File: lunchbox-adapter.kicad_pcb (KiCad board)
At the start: 2 copper layers, 67.6 x 89.2 mm, 91 parts, among them J1 Conn_01x24, J3 Conn_01x03, J4 Conn_01x03, J5 Conn_01x03, J6 Conn_01x06, J7 Conn_01x06, J8 Conn_01x03, Q1 SMBTA42, Q10 SMBTA42, Q11 SMBTA42, Q12 SMBTA42, Q2 SMBTA42, Q3 SMBTA42, Q4 SMBTA42, Q5 BCP51, Q6 SMBTA42, Q7 SMBTA42, Q8 SMBTA42, Q9 SMBTA42, U1 HCF4028B, U2 LM1117-5.0, U3 LM2904

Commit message: finished pcb design
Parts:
- turned C3 to 270 degrees
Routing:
- net START_BUTTON: track 57.9 -> 77.4 mm, vias 1 -> 2
- net GEAR_BCD_B: track 50.1 -> 65.8 mm, vias 1 -> 2
- net GEAR_BCD_A: track 49.3 -> 62.1 mm, vias 1 -> 2
- net +12V: track 75.0 -> 62.4 mm, vias 12 -> 16
- net SPD_12V: track 114.7 -> 124.8 mm, vias 1 -> 4
- net GEAR_BCD_C: track 50.4 -> 59.6 mm, vias 1 -> 2
- net Net-(J1-Pad15): track 25.9 -> 34.9 mm
- net SPEED_SENSOR: track 97.8 -> 105.5 mm, vias 1 -> 4
- net OIL_LAMP: track 75.8 -> 82.0 mm
- net SPD: track 10.6 -> 16.5 mm
- net VCC_Sensor: track 25.8 -> 20.5 mm, vias 1 -> 2
- net CHOKE_LAMP: track 76.3 -> 80.5 mm
- net RPM: track 16.5 -> 20.7 mm
- net TEMP_LAMP: track 76.4 -> 80.3 mm
- net GND: track 87.1 -> 90.3 mm
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
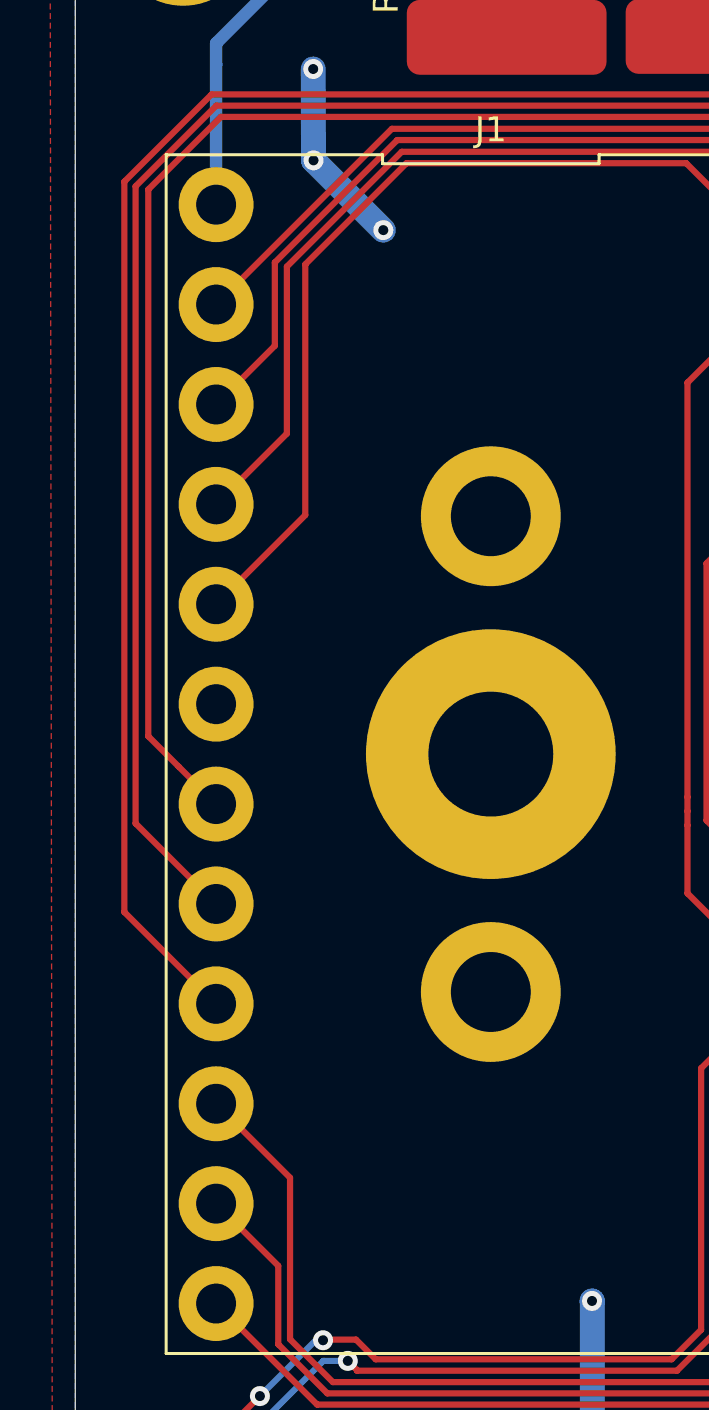
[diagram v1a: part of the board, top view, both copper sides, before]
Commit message: add schematic PDF
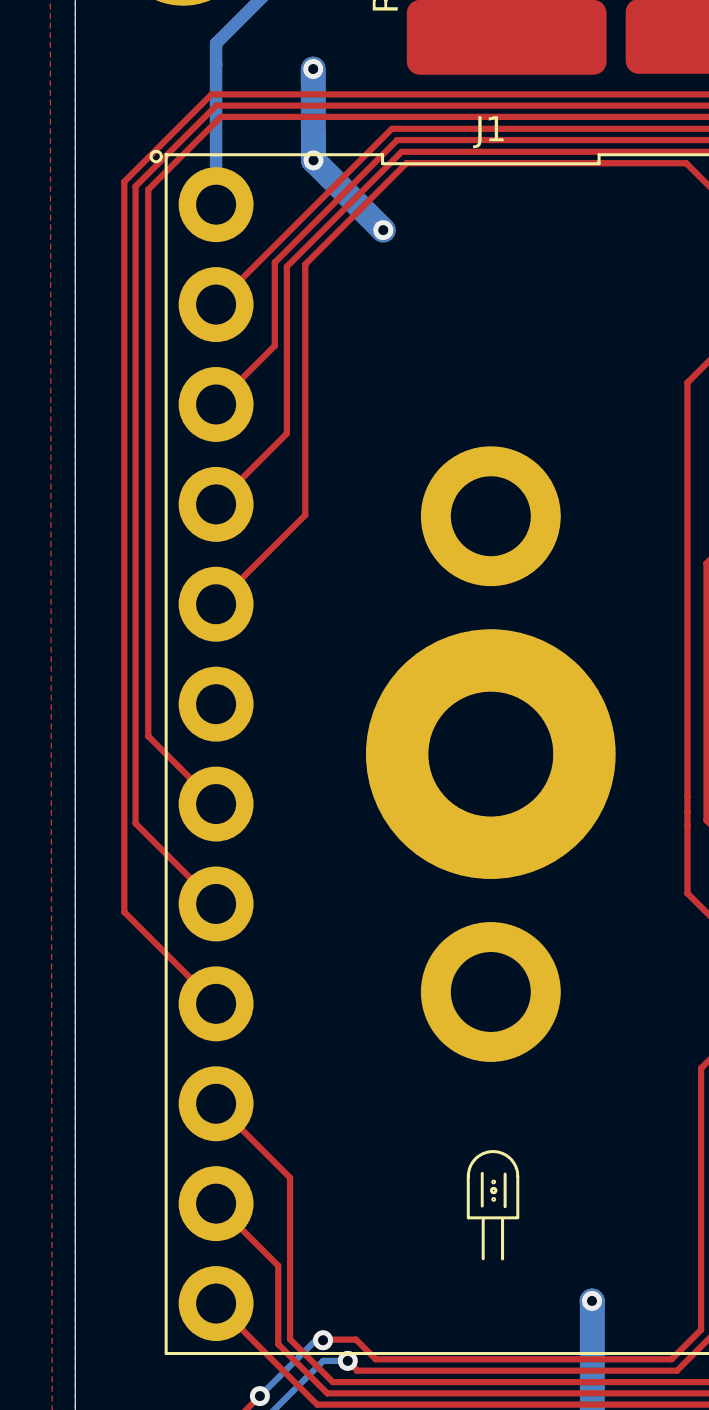
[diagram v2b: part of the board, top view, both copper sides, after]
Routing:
- net (no net): track 0.00 -> 5.80 mm, vias 0 -> 2
- net +12V: track 62.4 -> 56.6 mm, vias 16 -> 14
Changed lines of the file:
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@@
   (general
     (thickness 1.6)
-    (drawings 139)
+    (drawings 151)
     (tracks 649)
     (zones 0)
@@
     )
   )
+  (gr_circle (center 131.1783 103.6828) (end 131.214221 103.6828) (layer F.SilkS) (width 0.12))
+  (gr_circle (center 131.1783 102.9843) (end 131.214221 102.9843) (layer F.SilkS) (width 0.12))
+  (gr_circle (center 131.1783 103.3272) (end 131.268103 103.3272) (layer F.SilkS) (width 0.12))
+  (gr_line (start 131.6355 102.6668) (end 131.6355 103.9749) (layer F.SilkS) (width 0.12))
+  (gr_line (start 130.7211 102.6414) (end 130.7211 103.9495) (layer F.SilkS) (width 0.12))
+  (gr_line (start 131.5339 104.4575) (end 131.5339 106.0704) (layer F.SilkS) (width 0.12))
+  (gr_line (start 130.7592 104.4956) (end 130.7592 106.0577) (layer F.SilkS) (width 0.12))
+  (gr_line (start 132.1435 104.4067) (end 132.1435 102.7557) (layer F.SilkS) (width 0.12))
+  (gr_line (start 130.1623 104.4194) (end 132.1435 104.4194) (layer F.SilkS) (width 0.12))
+  (gr_line (start 130.1623 102.7557) (end 130.1623 104.4194) (layer F.SilkS) (width 0.12))
+  (gr_arc (start 131.1529 102.7557) (end 132.1435 102.7557) (angle -180) (layer F.SilkS) (width 0.12))
+  (gr_circle (center 117.6655 61.9252) (end 117.873795 61.9252) (layer F.SilkS) (width 0.12))
   (gr_line (start 171.2341 97.9043) (end 171.5516 97.7265) (layer F.SilkS) (width 0.12))
   (gr_line (start 171.5516 97.7265) (end 171.8818 97.8916) (layer F.SilkS) (width 0.12))
@@
   (via (at 150.241 93.853) (size 0.8) (drill 0.4) (layers F.Cu B.Cu) (net 3))
   (segment (start 150.241 97.282) (end 150.241 93.853) (width 1) (layer B.Cu) (net 3))
-  (via (at 135.128 113.538) (size 0.8) (drill 0.4) (layers F.Cu B.Cu) (net 3))
+  (via (at 135.128 113.538) (size 0.8) (drill 0.4) (layers F.Cu B.Cu) (net 0))
   (via (at 150.8887 70.3707) (size 0.8) (drill 0.4) (layers F.Cu B.Cu) (net 3))
   (segment (start 150.876 72.5535) (end 150.876 70.3834) (width 0.25) (layer F.Cu) (net 3))
@@
   (via (at 150.8887 67.0687) (size 0.8) (drill 0.4) (layers F.Cu B.Cu) (net 3))
   (segment (start 150.8887 70.3707) (end 150.8887 67.0687) (width 1) (layer B.Cu) (net 3))
-  (via (at 135.1153 107.7468) (size 0.8) (drill 0.4) (layers F.Cu B.Cu) (net 3))
-  (segment (start 135.128 107.7595) (end 135.1153 107.7468) (width 1) (layer B.Cu) (net 3))
-  (segment (start 135.128 113.538) (end 135.128 107.7595) (width 1) (layer B.Cu) (net 3))
+  (via (at 135.1153 107.7468) (size 0.8) (drill 0.4) (layers F.Cu B.Cu) (net 0))
+  (segment (start 135.128 107.7595) (end 135.1153 107.7468) (width 1) (layer B.Cu) (net 0))
+  (segment (start 135.128 113.538) (end 135.128 107.7595) (width 1) (layer B.Cu) (net 0))
   (via (at 153.3906 84.9249) (size 0.8) (drill 0.4) (layers F.Cu B.Cu) (net 3))
   (via (at 150.9014 84.9249) (size 0.8) (drill 0.4) (layers F.Cu B.Cu) (net 3))

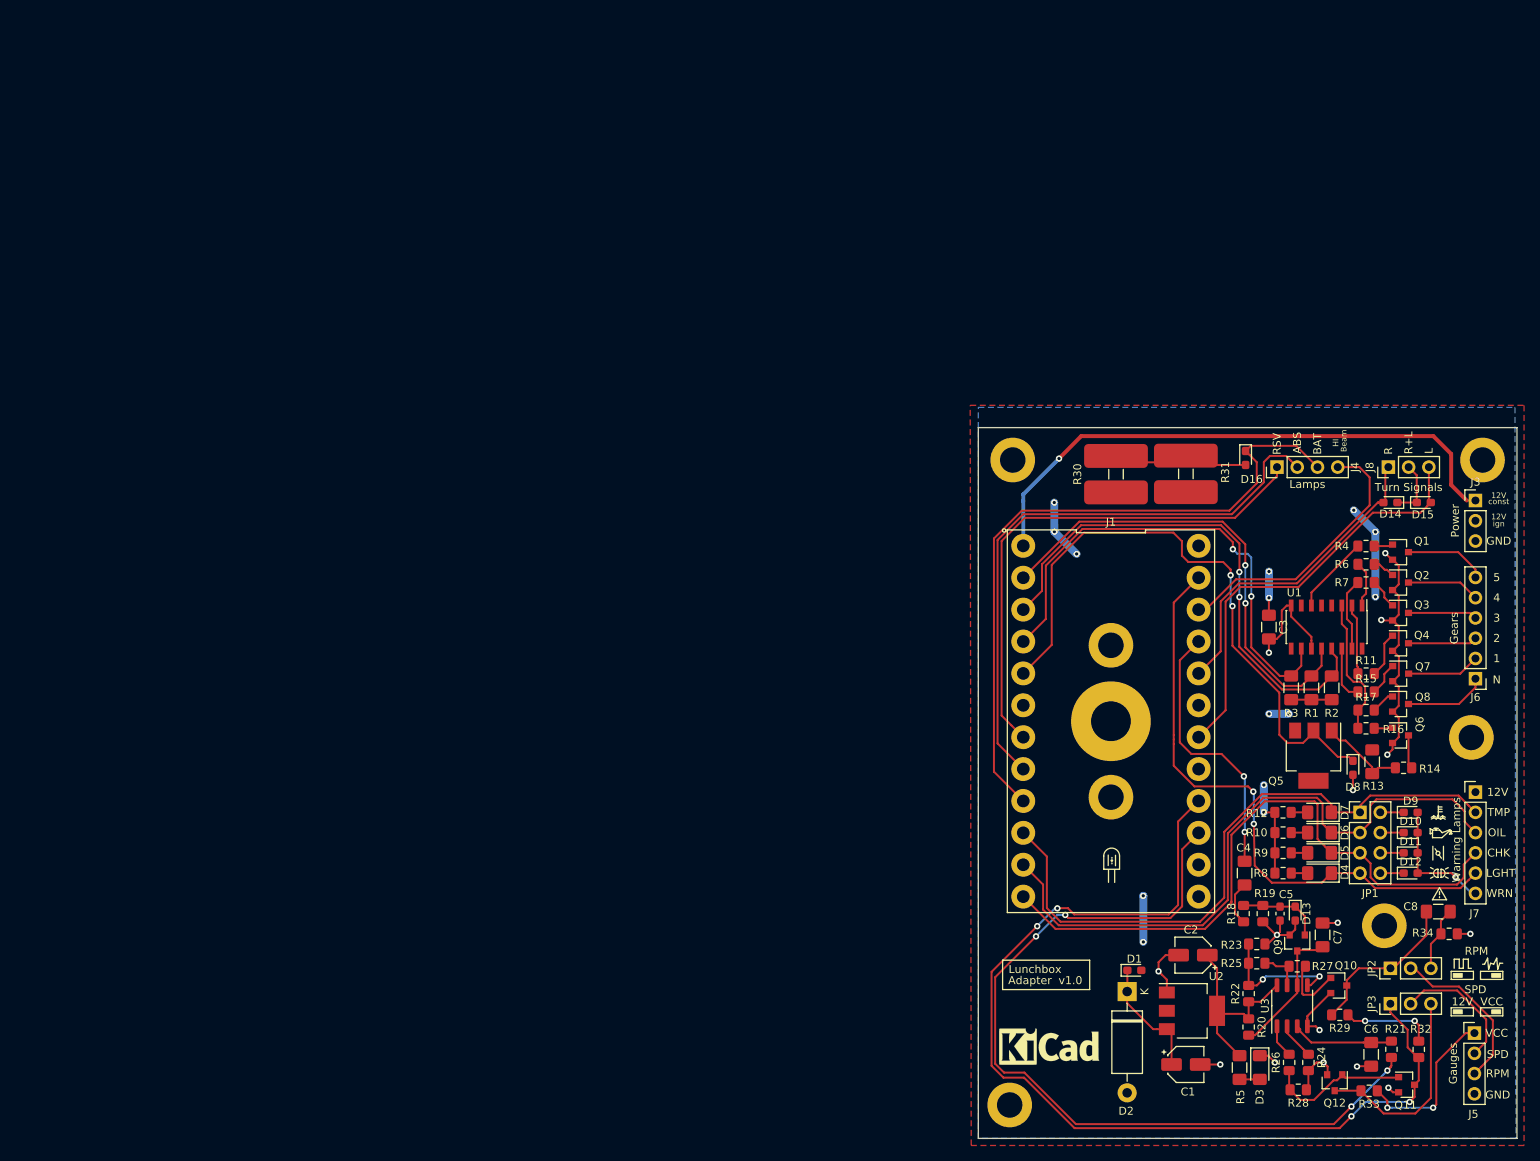
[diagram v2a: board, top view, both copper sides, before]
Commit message: change power resitor footprints, cleanup
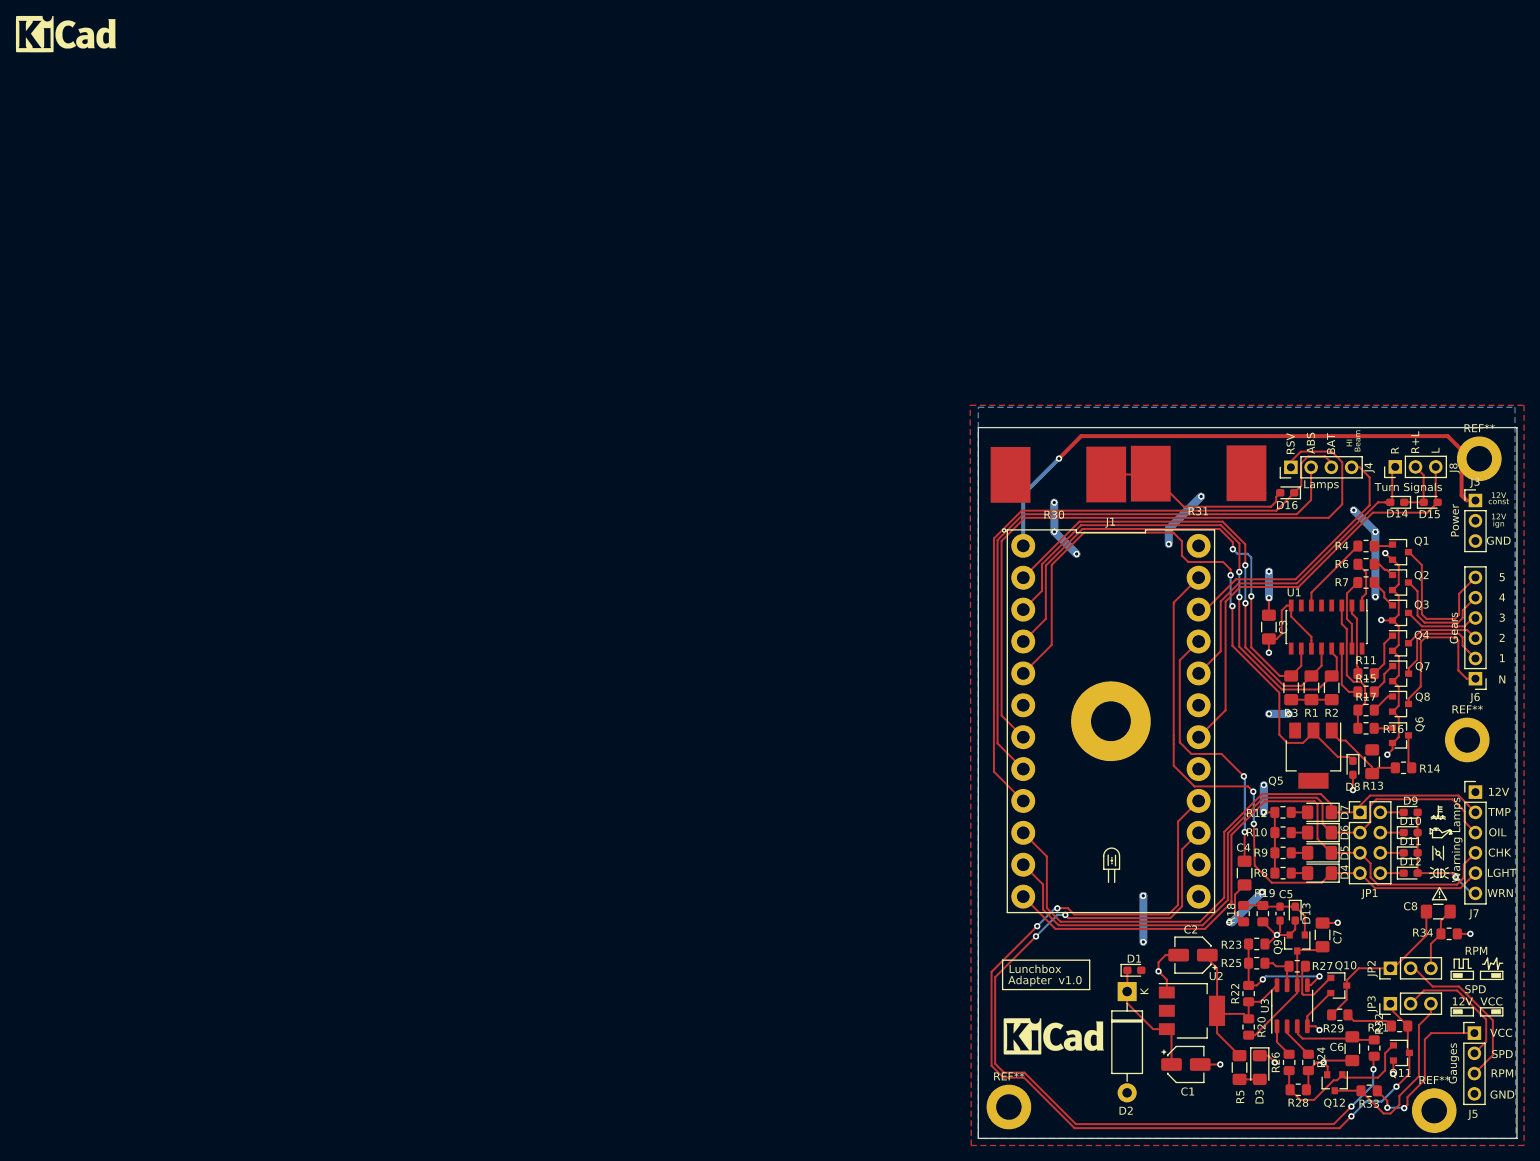
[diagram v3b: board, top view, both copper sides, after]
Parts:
- removed the REF** at (165.4, 111.5)
- removed the REF** at (177.7, 53.1)
- removed the REF** at (131.1, 76.3)
- removed the REF** at (131.1, 95.4)
- removed the REF** at (123.3, 127.0)
- removed the REF** at (118.7, 53.1)
- removed the REF** at (176.3, 87.9)
- removed the REF** at (118.4, 134.0)
- added REF**: MountingHole_3.2mm_M3_DIN965_Pad, MountingHole:MountingHole_3.2mm_M3_DIN965_Pad, F.Cu at (171.6, 134.7)
- added REF**: MountingHole_3.2mm_M3_DIN965_Pad, MountingHole:MountingHole_3.2mm_M3_DIN965_Pad, F.Cu at (118.3, 134.2)
- added REF**: MountingHole_3.2mm_M3_DIN965_Pad, MountingHole:MountingHole_3.2mm_M3_DIN965_Pad, F.Cu at (175.8, 88.2)
- added REF**: MountingHole_3.2mm_M3_DIN965_Pad, MountingHole:MountingHole_3.2mm_M3_DIN965_Pad, F.Cu at (177.3, 52.9)
- added REF**: KiCad-Logo_5mm_SilkScreen, bep:KiCad-Logo_5mm_SilkScreen, F.Cu at (123.9, 125.7)
- added REF**: KiCad-Logo_5mm_SilkScreen, bep:KiCad-Logo_5mm_SilkScreen, F.Cu at (0.00, 0.00)
- R30, R31: footprint Resistor_SMD:R_1206_3216Metric_Pad1.42x1.75mm_HandSolder -> bep:5020_resistor_thermal_pads
- moved R30 7.23 mm to (124.5, 54.9), turned to 0 degrees
- moved D16 6.81 mm to (153.2, 57.2), turned to 180 degrees
- moved Q11 4.04 mm to (167.5, 127.5)
- moved R32 3.79 mm to (167.3, 124.1), turned to 180 degrees
- moved C6 2.47 mm to (161.3, 126.9)
- moved R21 2.16 mm to (164.1, 126.8)
- moved J4 1.74 mm to (153.6, 54.0)
- moved R31 1.60 mm to (142.1, 54.8), turned to 180 degrees
- moved D15 0.86 mm to (171.2, 58.4)
- moved D14 0.86 mm to (167.0, 58.4)
- moved J8 0.86 mm to (166.7, 53.9)
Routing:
- net Net-(J1-Pad7): track 64.8 -> 83.9 mm
- net +12V: track 56.6 -> 67.9 mm, vias 14 -> 16
- net GEAR_N: track 10.4 -> 19.8 mm
- net GEAR_5: track 10.3 -> 19.2 mm
- net Net-(D16-Pad2): track 16.4 -> 24.6 mm
- net GEAR_1: track 9.17 -> 14.2 mm
- net GEAR_4: track 9.19 -> 14.1 mm
- net SPD_12V: track 124.8 -> 121.7 mm
- net Net-(Q11-Pad1): track 18.1 -> 20.4 mm
- net GND: track 90.3 -> 92.4 mm, vias 15 -> 14
- net Net-(C6-Pad1): track 12.9 -> 11.1 mm
- net Net-(JP3-Pad3): track 25.9 -> 24.1 mm
- net Net-(J1-Pad15): track 34.9 -> 33.2 mm
- net TURN_R: track 40.4 -> 42.0 mm
- net CHARGE_LAMP: track 85.3 -> 83.7 mm
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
